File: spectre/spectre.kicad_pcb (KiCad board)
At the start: 2 copper layers, 223 x 71 mm, 73 parts, among them J1 TC2030-IDC, J2 USB_B, K0 K00, K1 K00, K10 K00, K11 K00, K12 K00, K13 K00, K14 K00, K15 K00, K16 K00, K17 K00, K18 K00, K19 K00, K2 K00, K20 K00, K21 K00, K22 K00, K23 K00, K24 K00, K25 K00, K26 K00, K27 K00, K28 K00, K29 K00, K3 K00, K30 K00, K31 K00, K32 K00, K33 K00, K34 K00, K35 K00, K36 K00, K37 K00, K38 K00, K39 K00, K4 K00, K40 K00, K41 K00, K42 K00, K43 K00, K44 K00, K45 K00, K46 K00, K47 K00, K5 K00, K6 K00, K7 K00, K8 K00, K9 K00, U1 MIC550X, U2 ATXMEGA64A3U-MH

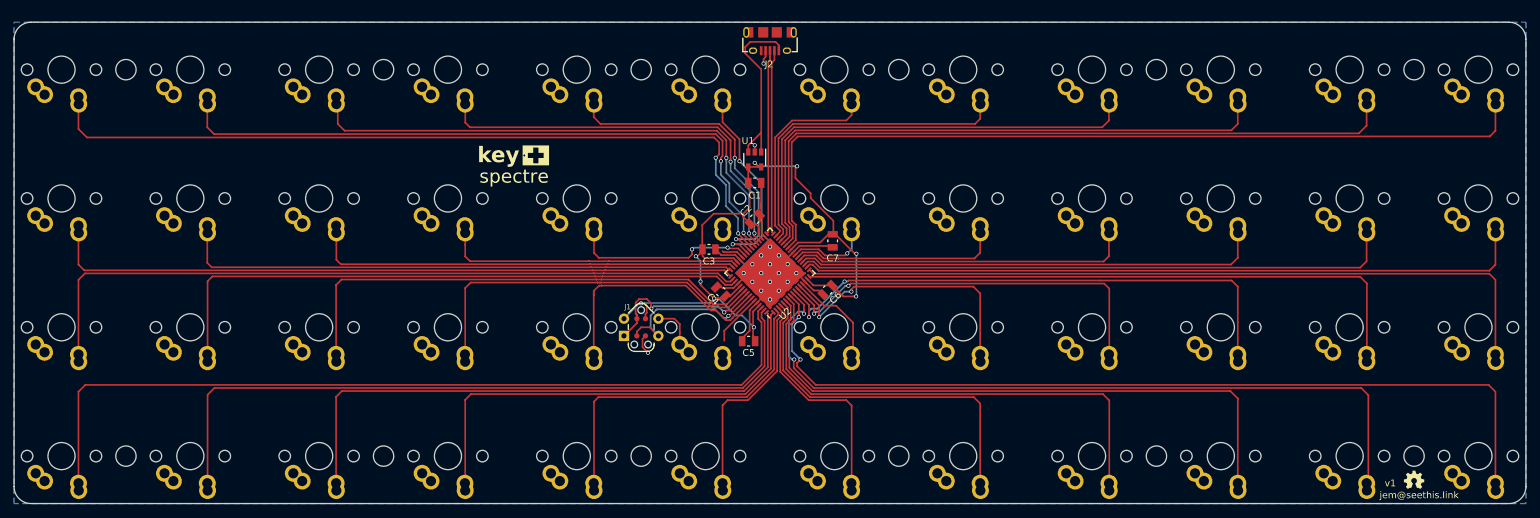
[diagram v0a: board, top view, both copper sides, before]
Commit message: add kailh low profile
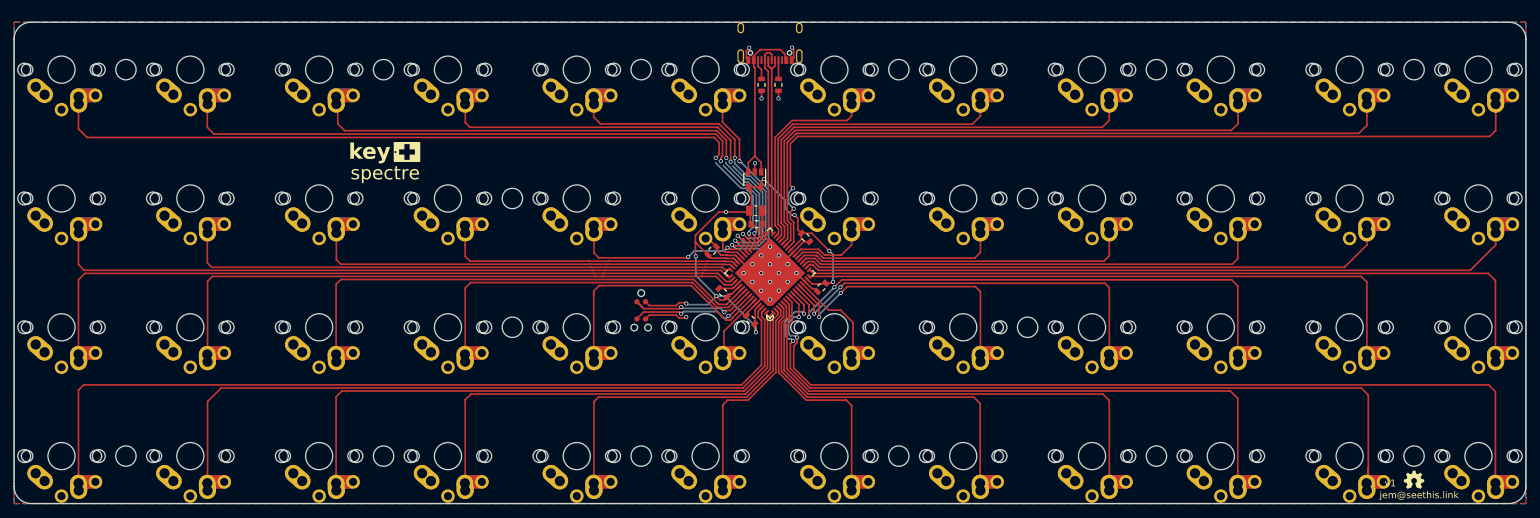
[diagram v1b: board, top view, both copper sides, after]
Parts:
- added R1: R, Resistor_SMD:R_0603_1608Metric, F.Cu at (110.2, 9.25)
- added R2: R, Resistor_SMD:R_0603_1608Metric, F.Cu at (112.8, 9.25)
- added REF**: MountingHole_3mm, mounting:MountingHole_3mm, F.Cu at (149.5, 45.0)
- added REF**: MountingHole_3mm, mounting:MountingHole_3mm, F.Cu at (149.5, 26.0)
- added REF**: MountingHole_3mm, mounting:MountingHole_3mm, F.Cu at (73.5, 26.0)
- added REF**: MountingHole_3mm, mounting:MountingHole_3mm, F.Cu at (73.5, 45.0)
- C2, C3, C4, C5, C6, C7: footprint Capacitor_SMD:C_0805_2012Metric -> Capacitor_SMD:C_0603_1608Metric
- J1: footprint Tag-Connect:TC2030-NL_SMALL_AND_IDC_PDI -> Tag-Connect:TC2030-NL_SMALL
- J2: value USB_B -> USB_Type_C_2.0_Receptacle; footprint conn_usb:USB_MicroB_Amphenol_10118194-0001LF -> conn_usb:USB_TypeC_U31F-24SNA0201
- K0, K1, K10, K11, K12, K13, K14, K15, K16, K17, K18, K19, K2, K20, K21, K22, K23, K24, K25, K26, K27, K28, K29, K3, K30, K31, K32, K33, K34, K35, K36, K37, K38, K39, K4, K40, K41, K42, K43, K44, K45, K46, K47, K5, K6, K7, K8, K9: footprint switch_mx:Cherry_MX_Matias_NoSilk.B -> switch_mx:Cherry_MX_Matias_KailhLP_NoSilk
- REF** (x12): footprint MountingHole:MountingHole_3mm -> mounting:MountingHole_3mm
- U2: footprint Package_DFN_QFN:QFN-64-1EP_9x9mm_P0.5mm -> qfn:QFN-64-1EP_9x9mm_P0.5mm
- moved ? 19.0 mm to (54.8, 19.2)
- moved C1 4.10 mm to (109.4, 27.8)
- moved C7 4.03 mm to (116.8, 31.8), turned to 135 degrees
- moved J2 3.25 mm to (111.5, -1.75)
- moved C5 3.18 mm to (108.6, 43.9), turned to 315 degrees
- moved U1 2.95 mm to (109.2, 23.2)
- moved J1 2.50 mm to (92.5, 42.5)
- moved C6 0.98 mm to (119.1, 39.1)
- moved C2 0.80 mm to (109.5, 29.8), turned to 180 degrees
- moved C3 0.53 mm to (103.0, 33.7), turned to 225 degrees
- moved C4 0.36 mm to (104.6, 39.9)
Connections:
- J2 pad S1: (no net) -> Net-(J2-PadS1)
- U1 pad 1: +5V -> VBUS
- U1 pad 3: +5V -> VBUS
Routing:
- net +5V: track 26.9 -> 0.00 mm
- net VBUS: track 0.00 -> 26.8 mm
- net VCC: track 124.6 -> 100.2 mm
- net GND: track 60.1 -> 49.1 mm, vias 19 -> 22
- net /RST: track 25.0 -> 19.2 mm, vias 1 -> 2
- net /PDI: track 25.2 -> 20.3 mm
- net /KEY46: track 112.3 -> 117.1 mm
- net /KEY0: track 116.9 -> 121.4 mm
- net /KEY1: track 97.8 -> 102.0 mm
- net /KEY4: track 46.0 -> 48.9 mm
- net Net-(J2-PadB5): track 0.00 -> 2.83 mm
- net Net-(J2-PadA5): track 0.00 -> 2.62 mm
- net /KEY17: track 3.37 -> 5.87 mm
- net /KEY5: track 29.4 -> 31.8 mm
- net /KEY29: track 7.83 -> 9.93 mm
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- added copper zone on F.Cu, net (none)
- removed copper zone on F.Cu, net GND
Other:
- net class Default: clearance 0.2 -> 0.16
- rule pad_to_mask_clearance: 0.03 -> 0.02
- rule trace_clearance: 0.2 -> 0.16

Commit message: update spectre BOM and move USB C port out farther
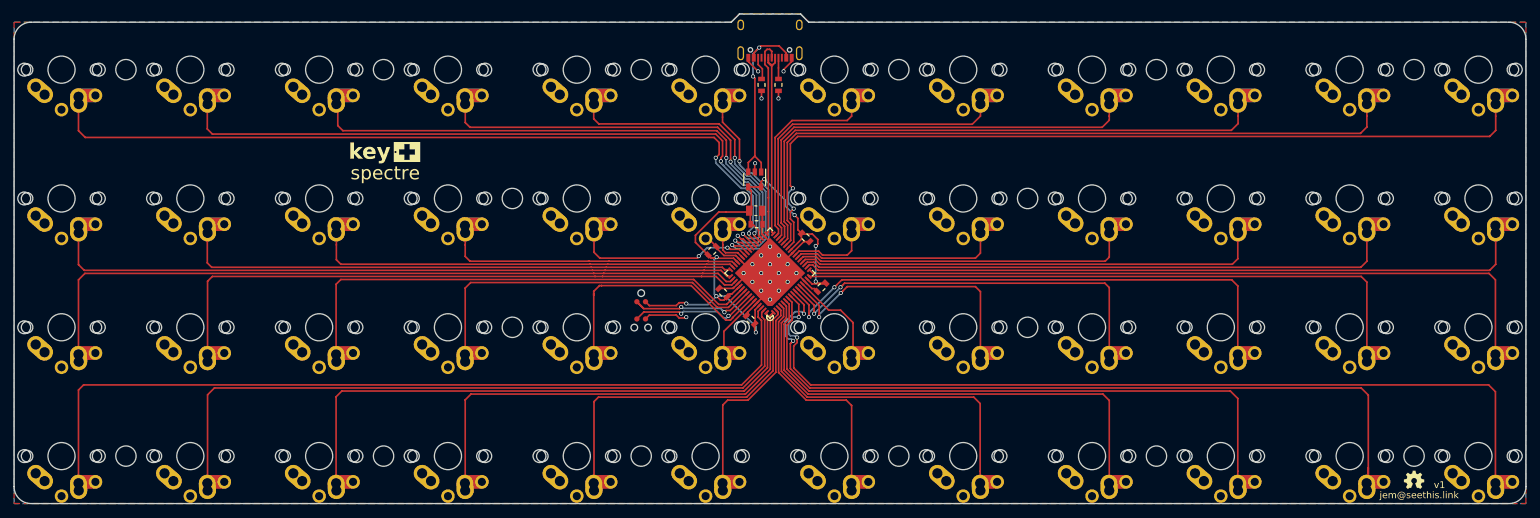
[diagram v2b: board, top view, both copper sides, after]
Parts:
- moved J2 0.45 mm to (111.5, -2.20)
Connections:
- net VBUS renamed +5V
- J2 pad S1: Net-(J2-PadS1) -> (no net)
- U2 pad 36: /KEY3 -> /KEY1
- U2 pad 37: /KEY2 -> /KEY0
- U2 pad 38: /KEY1 -> /KEY2
- U2 pad 39: /KEY0 -> /KEY3
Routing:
- net /KEY3: track 60.1 -> 66.8 mm
- net /KEY2: track 79.2 -> 83.4 mm
- net /KEY0: track 121.4 -> 117.6 mm
- net /KEY1: track 102.0 -> 98.5 mm
- net VCC: track 100.2 -> 97.3 mm, vias 9 -> 8
- net +5V: track 26.8 -> 29.7 mm, vias 0 -> 2
- net /D+: track 28.8 -> 31.0 mm
- net /KEY23: track 105.4 -> 107.1 mm
- net /KEY22: track 86.6 -> 88.0 mm
- net GND: track 49.1 -> 50.1 mm
- net /KEY37: track 106.1 -> 106.7 mm
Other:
- board size 223 x 71 mm -> 223 x 72.2 mm
